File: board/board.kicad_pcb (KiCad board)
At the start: 2 copper layers, 46.5 x 45 mm, 21 parts, among them J1 Conn_01x04_Pin, J2 Conn_01x04_Socket, J3 Conn_01x03_Socket, J4 Conn_01x02_Pin, U1 MSP430G2553IN20, U3 NCP1117-3.3_SOT223

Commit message: Updated PCB to use turbocase
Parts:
- added REF**: USB_C_Plug_JAE_DX07P024AJ1, Connector_USB:USB_C_Plug_JAE_DX07P024AJ1, F.Cu at (159.7, 72.3)
- moved H2 1.12 mm to (182.5, 62.0)
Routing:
- net ONE_WIRE_BUS: track 26.3 -> 29.6 mm

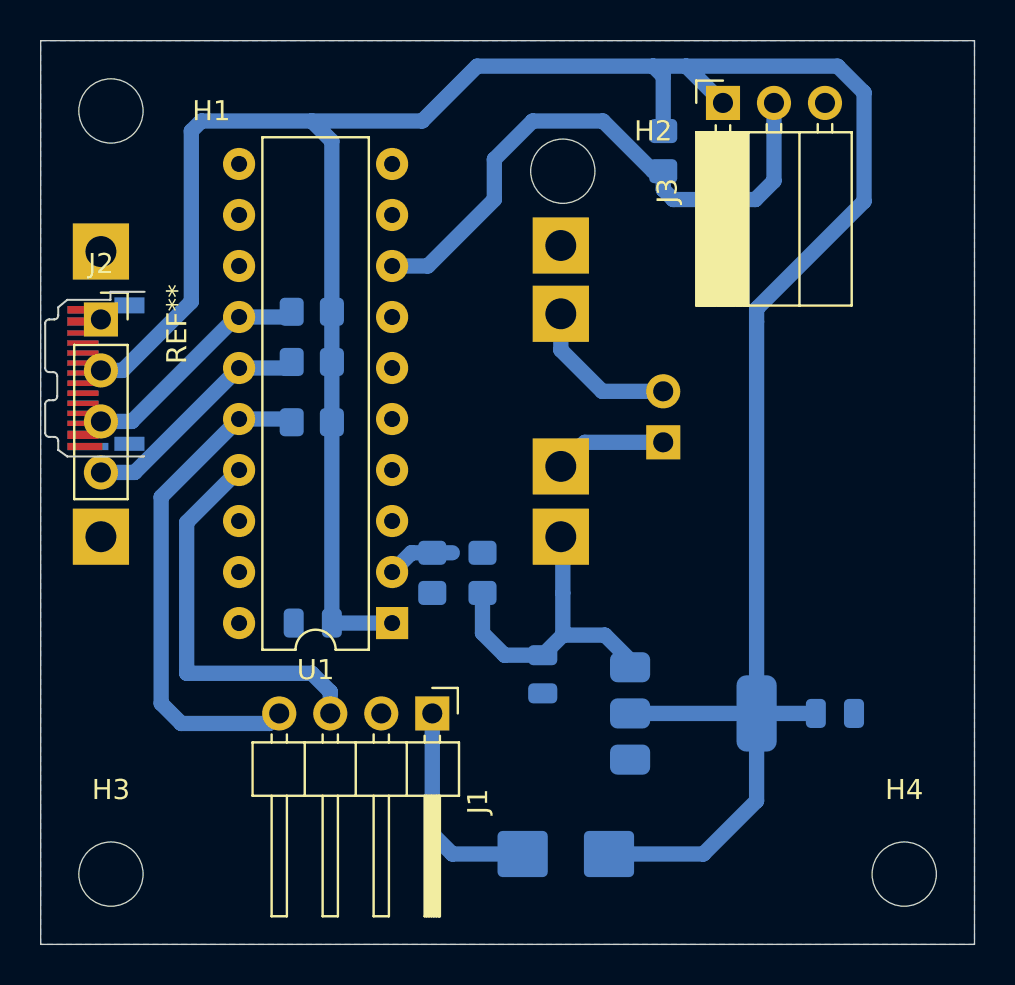
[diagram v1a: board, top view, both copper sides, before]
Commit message: Corrected sensor and oled pins
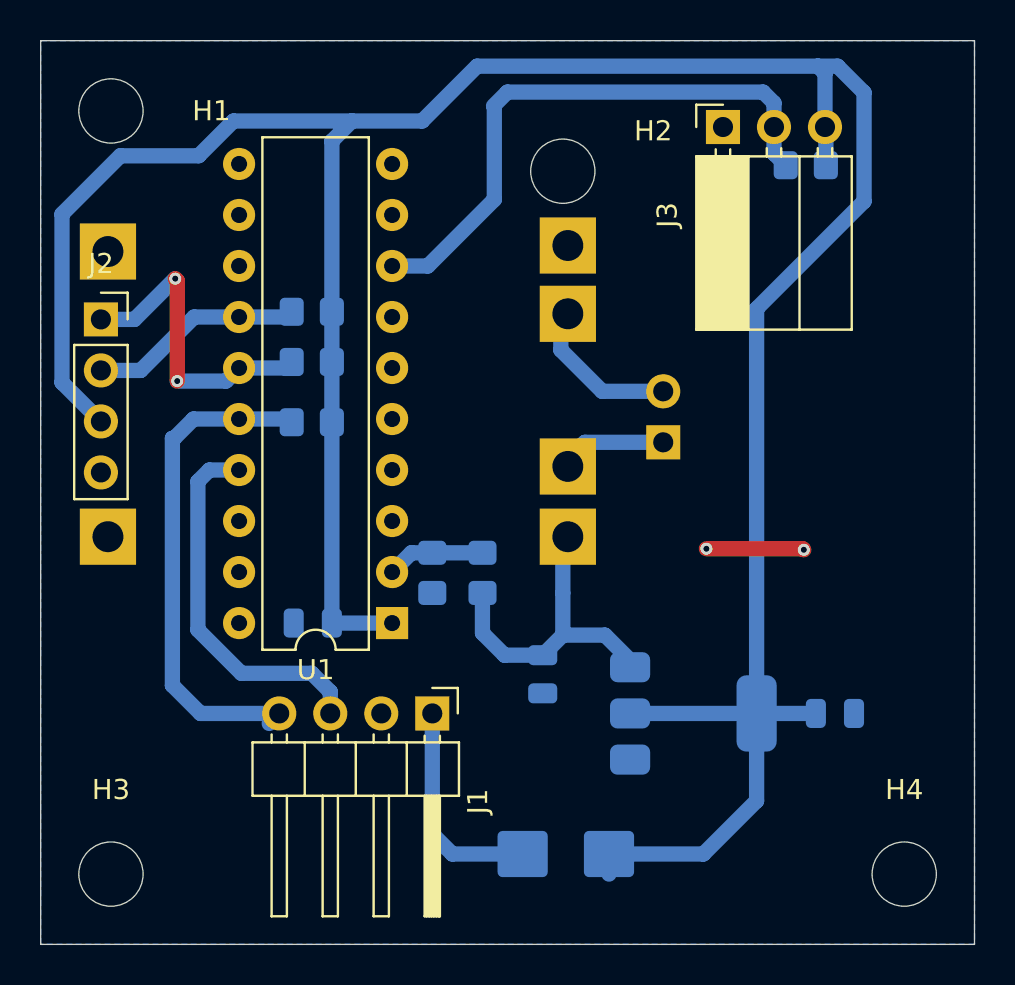
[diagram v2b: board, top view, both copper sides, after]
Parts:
- removed REF**: USB_C_Plug_JAE_DX07P024AJ1, Connector_USB:USB_C_Plug_JAE_DX07P024AJ1
- moved R2 7.13 mm to (194.6, 61.7), turned to 180 degrees
- moved J3 1.20 mm to (190.5, 59.8)
- moved U2 0.35 mm to (158.2, 81.9)
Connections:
- J2 pad 1: GND -> SDA
- J2 pad 2: +3.3V -> SCL
- J2 pad 3: SCL -> +3.3V
- J2 pad 4: SDA -> GND
- J3 pad 1: +3.3V -> GND
- J3 pad 3: GND -> +3.3V
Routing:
- net +3.3V: track 139.4 -> 144.4 mm
- net GND: track 0.00 -> 4.87 mm, vias 0 -> 2
- net SDA: track 11.8 -> 15.8 mm, vias 0 -> 2
- net BAT_VOLTAGE: track 3.40 -> 4.90 mm
- net SBWTCK: track 19.8 -> 18.6 mm
- net SCL: track 12.1 -> 11.1 mm
- net ONE_WIRE_BUS: track 29.6 -> 28.9 mm
